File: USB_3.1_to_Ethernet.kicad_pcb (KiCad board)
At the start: 4 copper layers, 75 x 25 mm, 10 parts, among them J1 RJ45_JK0654219, J2 USB3_A, U1 LAN7801_9JX, U2 93LC56B_SN, U3 KSZ9031RNXCC, U4 TLV76733QWDRBxQ1, U5 USBLC6-2P6, U6 TPS7A0230PDQNR, Y1 C3E-8.000-18-3030-R

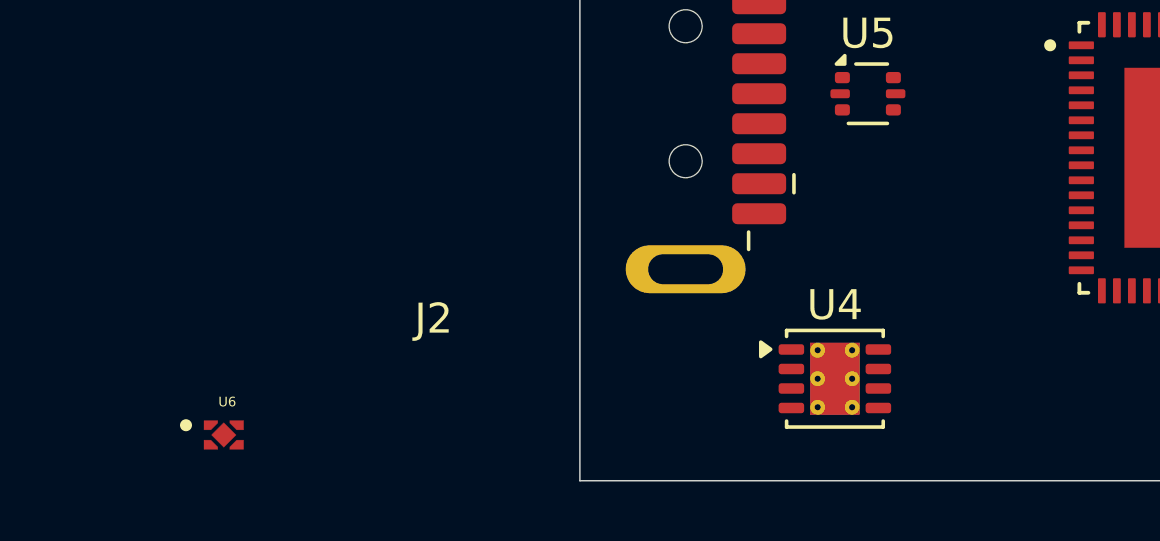
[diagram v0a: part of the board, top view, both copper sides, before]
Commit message: power section added and power connections made
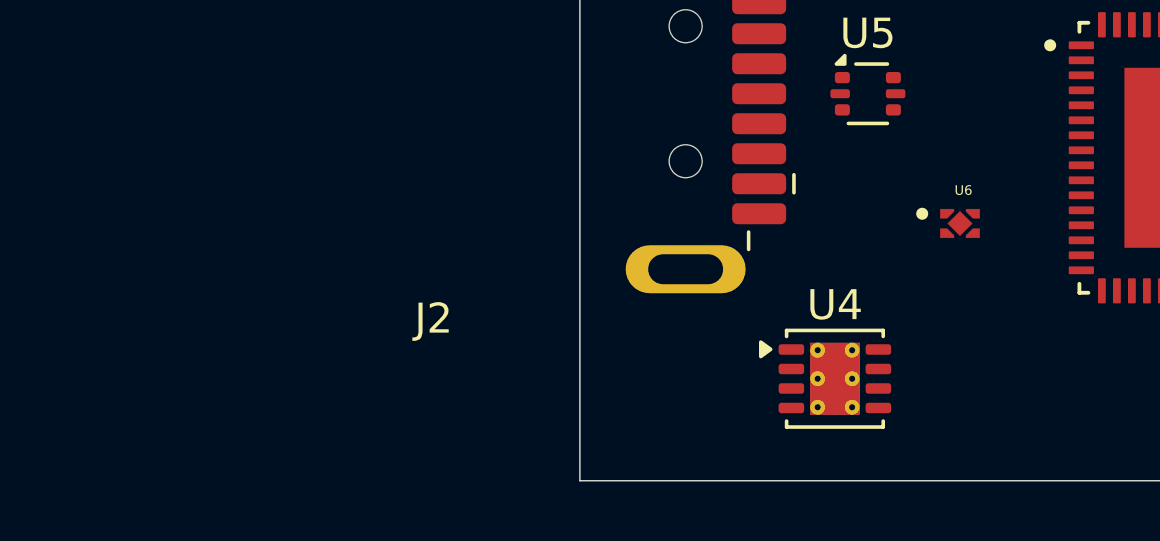
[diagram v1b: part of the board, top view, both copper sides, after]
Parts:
- moved U6 25.5 mm to (72.4, 66.5)
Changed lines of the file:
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@@
 	(footprint "TPS7A0230PDQNR:IC_TPS7A0230PDQNR"
 		(layer "F.Cu")
-		(at 47.83 73.575)
+		(at 72.37 66.525)
 		(property "Reference" "U6"
 			(at 0.116 -1.1032 0)

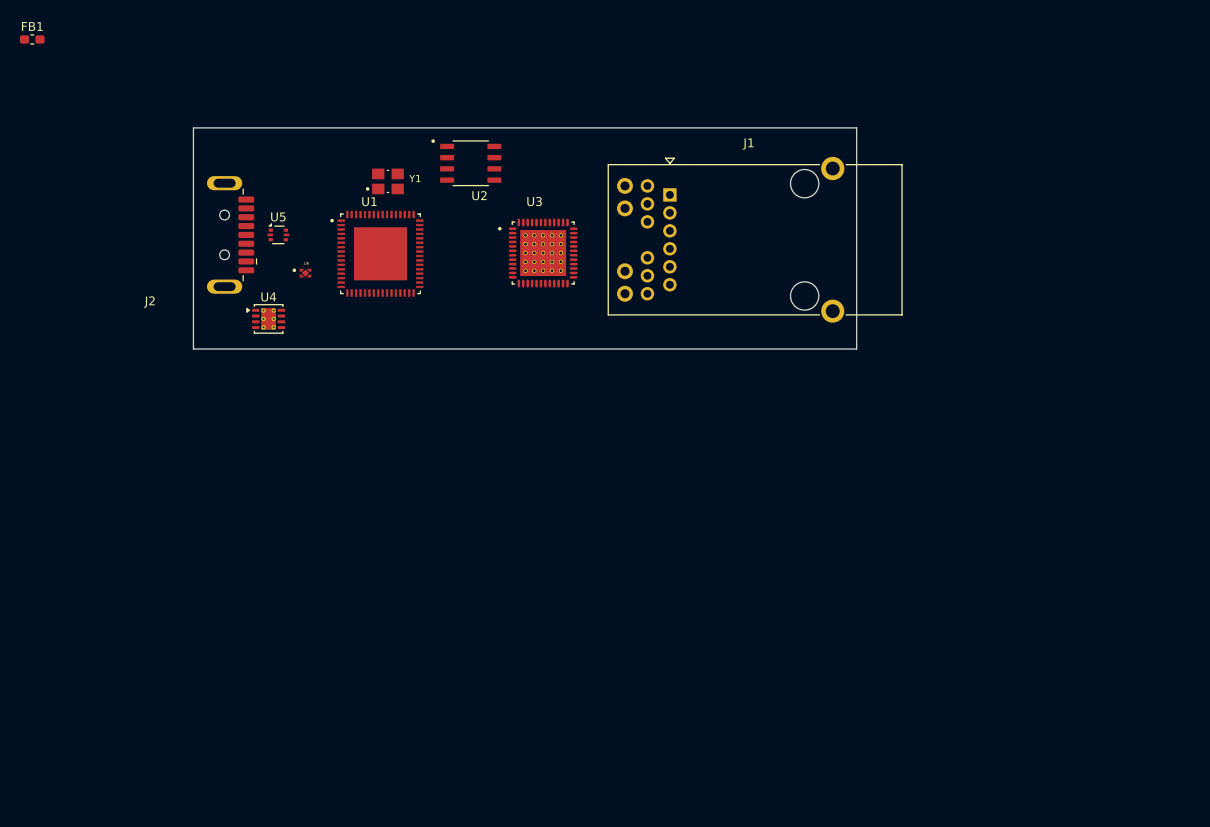
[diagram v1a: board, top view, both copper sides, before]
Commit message: usb connections done without 27 ohm, SMI connections done, EEPROM connections done.
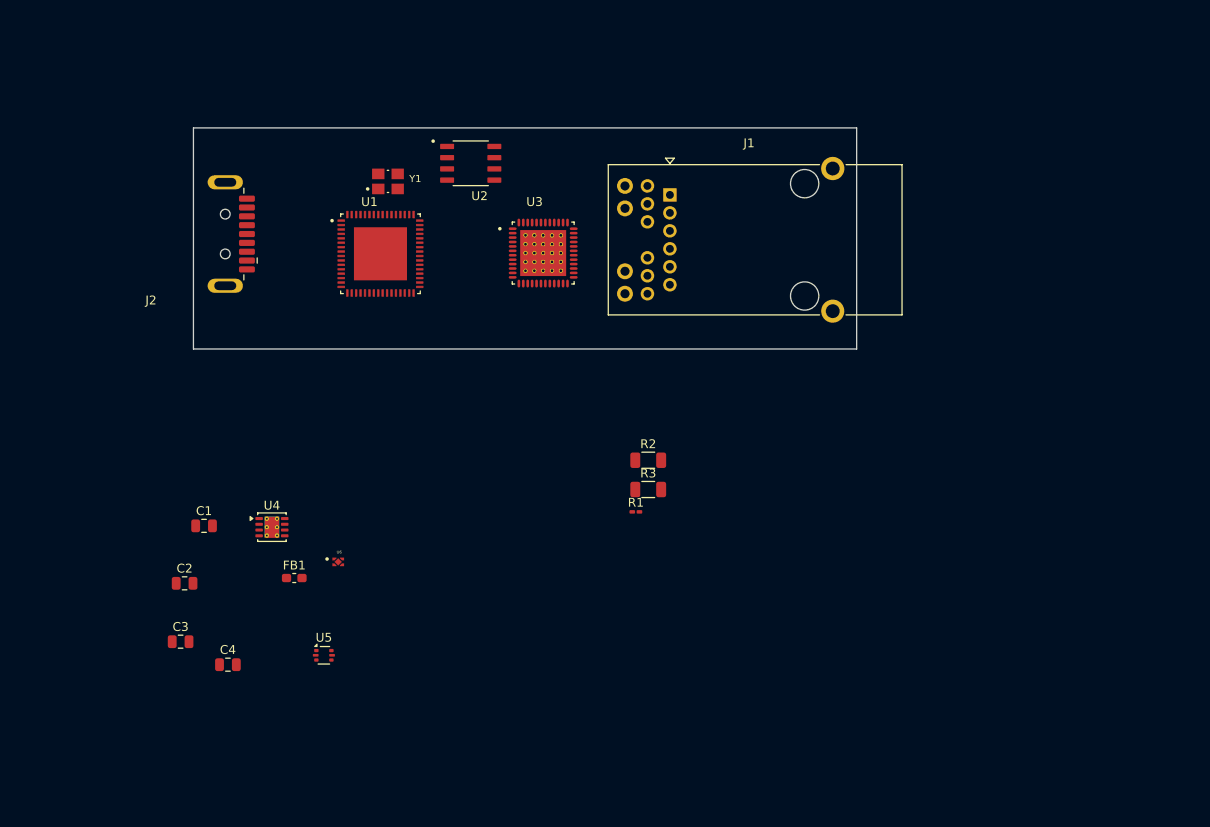
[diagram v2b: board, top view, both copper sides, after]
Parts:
- added C1: 1uF, Capacitor_SMD:C_0805_2012Metric, F.Cu at (60.9, 95.1)
- added C2: 1uF, Capacitor_SMD:C_0805_2012Metric, F.Cu at (58.7, 101.6)
- added C3: 1uF, Capacitor_SMD:C_0805_2012Metric, F.Cu at (58.2, 108.2)
- added C4: 1uF, Capacitor_SMD:C_0805_2012Metric, F.Cu at (63.6, 110.8)
- added R1: 12K, Resistor_SMD:R_0201_0603Metric_Pad0.64x0.40mm_HandSolder, F.Cu at (109.7, 93.5)
- added R2: 1.5K, Resistor_SMD:R_1206_3216Metric, F.Cu at (111.1, 87.7)
- added R3: 1.5K, Resistor_SMD:R_1206_3216Metric, F.Cu at (111.1, 91.0)
- U4: value TLV76733QWDRBxQ1 -> TLV76733
- U6: value TPS7A0230PDQNR -> TPS7A0212
- Y1: value C3E-8.000-18-3030-R -> 125MHz
- moved FB1 67.7 mm to (71.1, 101.0)
- moved U5 47.8 mm to (74.5, 109.7)
- moved U6 32.9 mm to (76.1, 99.2)
- moved U4 23.6 mm to (68.6, 95.2)
- moved J2 0.12 mm to (54.9, 62.1)
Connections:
- FB1 pad 1: unconnected-(FB1-Pad1) -> VBUS
- FB1 pad 2: unconnected-(FB1-Pad2) -> +5V
- J2 pad 1: unconnected-(J2-VBUS-Pad1) -> VBUS
- J2 pad 10: unconnected-(J2-SHIELD-Pad10) -> GND
- J2 pad 2: unconnected-(J2-D--Pad2) -> Net-(J2-D-)
- J2 pad 3: unconnected-(J2-D+-Pad3) -> Net-(J2-D+)
- J2 pad 4: unconnected-(J2-GND-Pad4) -> GND
- J2 pad 5: unconnected-(J2-SSRX--Pad5) -> SSRX-
- J2 pad 6: unconnected-(J2-SSRX+-Pad6) -> SSRX+
- J2 pad 7: unconnected-(J2-DRAIN-Pad7) -> GND
- J2 pad 8: unconnected-(J2-SSTX--Pad8) -> SSTX-
- J2 pad 9: unconnected-(J2-SSTX+-Pad9) -> SSTX+
- U1 pad 11: VDDVARIO -> 3v3_out
- U1 pad 18: VDDVARIO -> 3v3_out
- U1 pad 21: unconnected-(U1-VDD_SW_IN-Pad21) -> 3v3_out
- U1 pad 23: unconnected-(U1-EECS/GPIO0-Pad23) -> /CS
- U1 pad 24: unconnected-(U1-EEDI/GPIO1-Pad24) -> /DI
- U1 pad 25: unconnected-(U1-EEDO/GPIO2-Pad25) -> /DO
- U1 pad 26: unconnected-(U1-EECLK/GPIO3-Pad26) -> /CLK
- U1 pad 27: VDDVARIO -> 3v3_out
- U1 pad 3: VDDVARIO -> 3v3_out
- U1 pad 38: unconnected-(U1-USB2_DP-Pad38) -> D+
- U1 pad 39: unconnected-(U1-USB2_DM-Pad39) -> D-
- U1 pad 40: unconnected-(U1-USB3_TXDP-Pad40) -> SSTX+
- U1 pad 41: unconnected-(U1-USB3_TXDM-Pad41) -> SSTX-
- U1 pad 43: unconnected-(U1-USB3_RXDP-Pad43) -> SSRX+
- U1 pad 44: unconnected-(U1-USB3_RXDM-Pad44) -> SSRX-
- U1 pad 48: VDDVARIO -> 3v3_out
- U1 pad 49: unconnected-(U1-USBRBIAS-Pad49) -> Net-(U1-USBRBIAS)
- U1 pad 50: unconnected-(U1-VDD33A-Pad50) -> 3v3_out
- U1 pad 51: VDDVARIO -> 3v3_out
- U1 pad 52: unconnected-(U1-XI-Pad52) -> /XI
- U1 pad 53: unconnected-(U1-XO-Pad53) -> /XO
- U1 pad 55: unconnected-(U1-MDIO-Pad55) -> /MDIO
- U1 pad 56: unconnected-(U1-MDC-Pad56) -> /MDC
- U1 pad 64: unconnected-(U1-VDD33_REG_IN-Pad64) -> 3v3_out
- U1 pad 65: unconnected-(U1-VSS-Pad65) -> GND
- U1 pad 7: VDDVARIO -> 3v3_out
- U2 pad 1: unconnected-(U2-CS-Pad1) -> /CS
- U2 pad 2: unconnected-(U2-CLK-Pad2) -> /CLK
- U2 pad 3: unconnected-(U2-DI-Pad3) -> /DI
- U2 pad 4: unconnected-(U2-DO-Pad4) -> /DO
- U2 pad 5: unconnected-(U2-VSS-Pad5) -> GND
- U2 pad 6: Net-(U2-NC-Pad6) -> unconnected-(U2-NC-Pad6)_1
- U2 pad 7: Net-(U2-NC-Pad6) -> unconnected-(U2-NC-Pad6)
- U2 pad 8: unconnected-(U2-VCC-Pad8) -> 3v3_out
- U3 pad 1: AVDDH -> 3v3_out
- U3 pad 12: AVDDH -> 3v3_out
- U3 pad 14: DVDDL -> 1v2_core
- U3 pad 16: DVDDH -> 3v3_out
- U3 pad 18: DVDDL -> 1v2_core
- U3 pad 23: DVDDL -> 1v2_core
- U3 pad 26: DVDDL -> 1v2_core
- U3 pad 29: unconnected-(U3-VSS-Pad29) -> GND
- U3 pad 30: DVDDL -> 1v2_core
- U3 pad 34: DVDDH -> 3v3_out
- U3 pad 36: unconnected-(U3-MDC-Pad36) -> /MDC
- U3 pad 37: unconnected-(U3-MDIO-Pad37) -> /MDIO
- U3 pad 39: DVDDL -> 1v2_core
- U3 pad 4: AVDDL -> 1v2_core
- U3 pad 40: DVDDH -> 3v3_out
- U3 pad 49: P_GND -> GND
- U3 pad 49_1: P_GND -> GND
- U3 pad 49_10: P_GND -> GND
- U3 pad 49_11: P_GND -> GND
- U3 pad 49_12: P_GND -> GND
- U3 pad 49_13: P_GND -> GND
- U3 pad 49_14: P_GND -> GND
- U3 pad 49_15: P_GND -> GND
- U3 pad 49_16: P_GND -> GND
- U3 pad 49_17: P_GND -> GND
- U3 pad 49_18: P_GND -> GND
- U3 pad 49_19: P_GND -> GND
- U3 pad 49_2: P_GND -> GND
- U3 pad 49_20: P_GND -> GND
- U3 pad 49_21: P_GND -> GND
- U3 pad 49_22: P_GND -> GND
- U3 pad 49_23: P_GND -> GND
- U3 pad 49_24: P_GND -> GND
- U3 pad 49_25: P_GND -> GND
- U3 pad 49_3: P_GND -> GND
- U3 pad 49_4: P_GND -> GND
- U3 pad 49_5: P_GND -> GND
- U3 pad 49_6: P_GND -> GND
- U3 pad 49_7: P_GND -> GND
- U3 pad 49_8: P_GND -> GND
- U3 pad 49_9: P_GND -> GND
- U3 pad 9: AVDDL -> 1v2_core
- U4 pad 1: unconnected-(U4-OUT-Pad1) -> 3v3_out
- U4 pad 3: unconnected-(U4-SNS-Pad3) -> 3v3_out
- U4 pad 4: Net-(U4-GND-Pad4) -> GND
- U4 pad 5: unconnected-(U4-EN-Pad5) -> +5V
- U4 pad 6: Net-(U4-GND-Pad4) -> GND
- U4 pad 8: unconnected-(U4-IN-Pad8) -> +5V
- U4 pad 9: unconnected-(U4-PAD-Pad9) -> GND
- U5 pad 1: unconnected-(U5-I/O1-Pad1) -> Net-(J2-D-)
- U5 pad 2: unconnected-(U5-GND-Pad2) -> GND
- U5 pad 3: unconnected-(U5-I/O2-Pad3) -> Net-(J2-D+)
- U5 pad 4: unconnected-(U5-I/O2-Pad4) -> D+
- U5 pad 5: unconnected-(U5-VBUS-Pad5) -> +5V
- U5 pad 6: unconnected-(U5-I/O1-Pad6) -> D-
- U6 pad 1: unconnected-(U6-OUT-Pad1) -> 1v2_core
- U6 pad 2: unconnected-(U6-GND-Pad2) -> GND
- U6 pad 3: unconnected-(U6-EN-Pad3) -> +5V
- U6 pad 4: unconnected-(U6-IN-Pad4) -> +5V
- U6 pad 5: unconnected-(U6-THERMAL_PAD-Pad5) -> GND
- Y1 pad 1: unconnected-(Y1-Pad1) -> /XI
- Y1 pad 3: unconnected-(Y1-Pad3) -> /XO

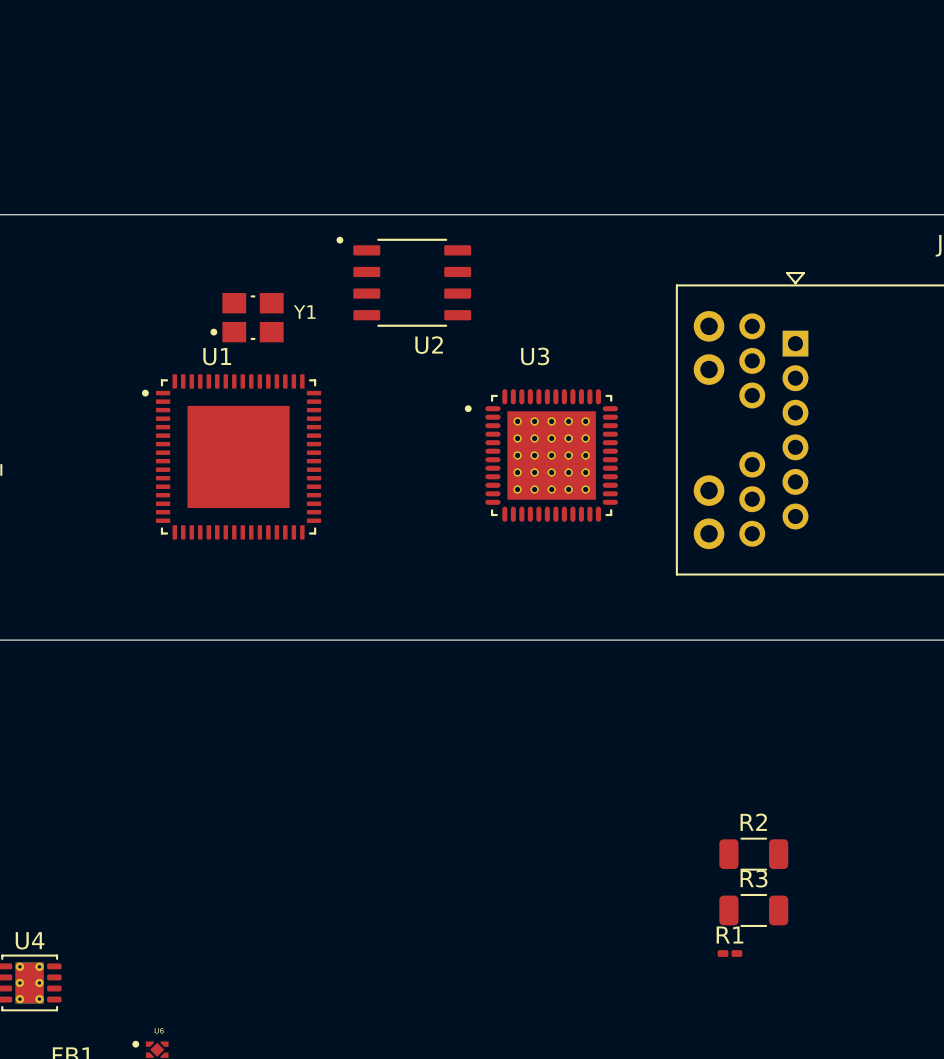
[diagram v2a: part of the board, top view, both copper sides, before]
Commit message: RGMII connections made, Clk circuitry made, 27 ohm resistors added
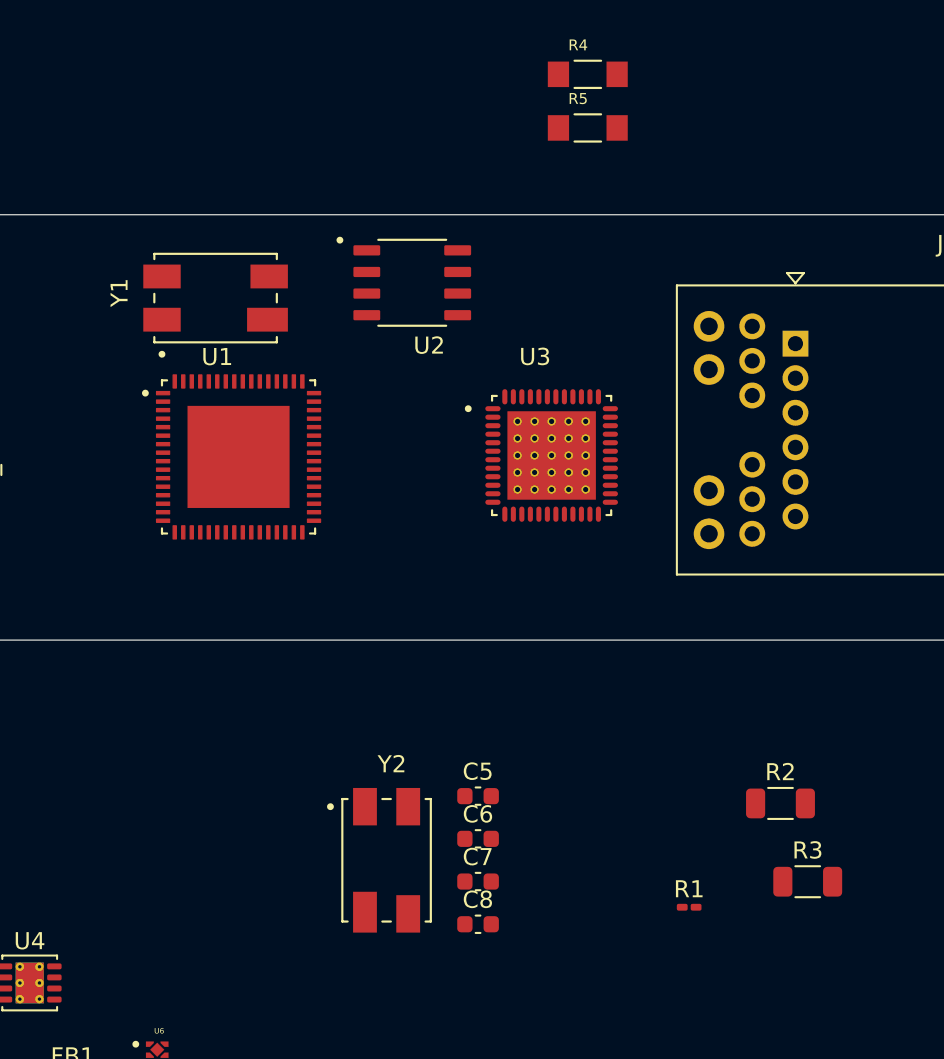
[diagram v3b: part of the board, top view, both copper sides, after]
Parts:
- added C5: 22pF, Capacitor_SMD:C_0603_1608Metric, F.Cu at (94.9, 84.3)
- added C6: 22pF, Capacitor_SMD:C_0603_1608Metric, F.Cu at (94.9, 86.8)
- added C7: 22pF, Capacitor_SMD:C_0603_1608Metric, F.Cu at (94.9, 89.3)
- added C8: 22pF, Capacitor_SMD:C_0603_1608Metric, F.Cu at (94.9, 91.8)
- added R4: 27R, Resistor_SMD:R_1206, F.Cu at (101.4, 41.9)
- added R5: 27R, Resistor_SMD:R_1206, F.Cu at (101.4, 45.0)
- added Y2: 25MHz, Crystal:XTAL_ABMM325000MHZET, F.Cu at (89.5, 88.0)
- Y1: value 125MHz -> 25MHz; footprint C3E-8.000-18-3030-R:XTAL_C3E-8.000-18-3030-R -> Crystal:XTAL_ABMM325000MHZET
- moved R1 3.63 mm to (107.3, 90.8)
- moved R3 3.59 mm to (114.3, 89.3)
- moved R2 3.37 mm to (112.7, 84.7)
- moved Y1 2.48 mm to (79.5, 55.0), turned to 90 degrees
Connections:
- net /XI renamed /XI_LAN
- net /XO renamed /XO_LAN
- U1 pad 10: unconnected-(U1-TXC-Pad10) -> /TXC
- U1 pad 12: unconnected-(U1-RXC-Pad12) -> /RXC
- U1 pad 13: unconnected-(U1-RX_CTL-Pad13) -> /RX_CTL
- U1 pad 14: unconnected-(U1-RXD0-Pad14) -> /RXD0
- U1 pad 15: unconnected-(U1-RXD1-Pad15) -> /RXD1
- U1 pad 16: unconnected-(U1-RXD2-Pad16) -> /RXD2
- U1 pad 17: unconnected-(U1-RXD3-Pad17) -> /RXD3
- U1 pad 4: unconnected-(U1-TXD3-Pad4) -> /TXD3
- U1 pad 5: unconnected-(U1-TXD2-Pad5) -> /TXD2
- U1 pad 6: unconnected-(U1-TXD1-Pad6) -> /TXD1
- U1 pad 8: unconnected-(U1-TXD0-Pad8) -> /TXD0
- U1 pad 9: unconnected-(U1-TX_CTL-Pad9) -> /TX_CTL
- U3 pad 19: unconnected-(U3-TXD0-Pad19) -> /RXD0
- U3 pad 20: unconnected-(U3-TXD1-Pad20) -> /RXD1
- U3 pad 21: unconnected-(U3-TXD2-Pad21) -> /RXD2
- U3 pad 22: unconnected-(U3-TXD3-Pad22) -> /RXD3
- U3 pad 24: unconnected-(U3-GTX_CLK-Pad24) -> /TXC
- U3 pad 25: unconnected-(U3-TX_EN-Pad25) -> /TX_CTL
- U3 pad 27: unconnected-(U3-RXD3/MODE3-Pad27) -> /TXD3
- U3 pad 28: unconnected-(U3-RXD2/MODE2-Pad28) -> /TXD2
- U3 pad 31: unconnected-(U3-RXD1/MODE1-Pad31) -> /TXD1
- U3 pad 32: unconnected-(U3-RXD0/MODE0-Pad32) -> /TXD0
- U3 pad 33: unconnected-(U3-RX_DV/CLK125_EN-Pad33) -> /RX_CTL
- U3 pad 35: unconnected-(U3-RX_CLK/PHYAD2-Pad35) -> /RXC
- U3 pad 45: unconnected-(U3-XO-Pad45) -> /XO_PHY
- U3 pad 46: unconnected-(U3-XI-Pad46) -> /XI_PHY
- U5 pad 4: D+ -> Net-(R5-Pad1)
- U5 pad 6: D- -> Net-(R4-Pad1)
